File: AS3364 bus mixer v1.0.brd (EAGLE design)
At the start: 44.5 x 30.5 mm, 96 parts, among them IC1 TL072JT, IC2 TL072JT, IC3 TL072JT, IC30 TL072JT, IC4 TL072JT, IC5 79L09F, IC6 78L09F, IC7 CH446Q

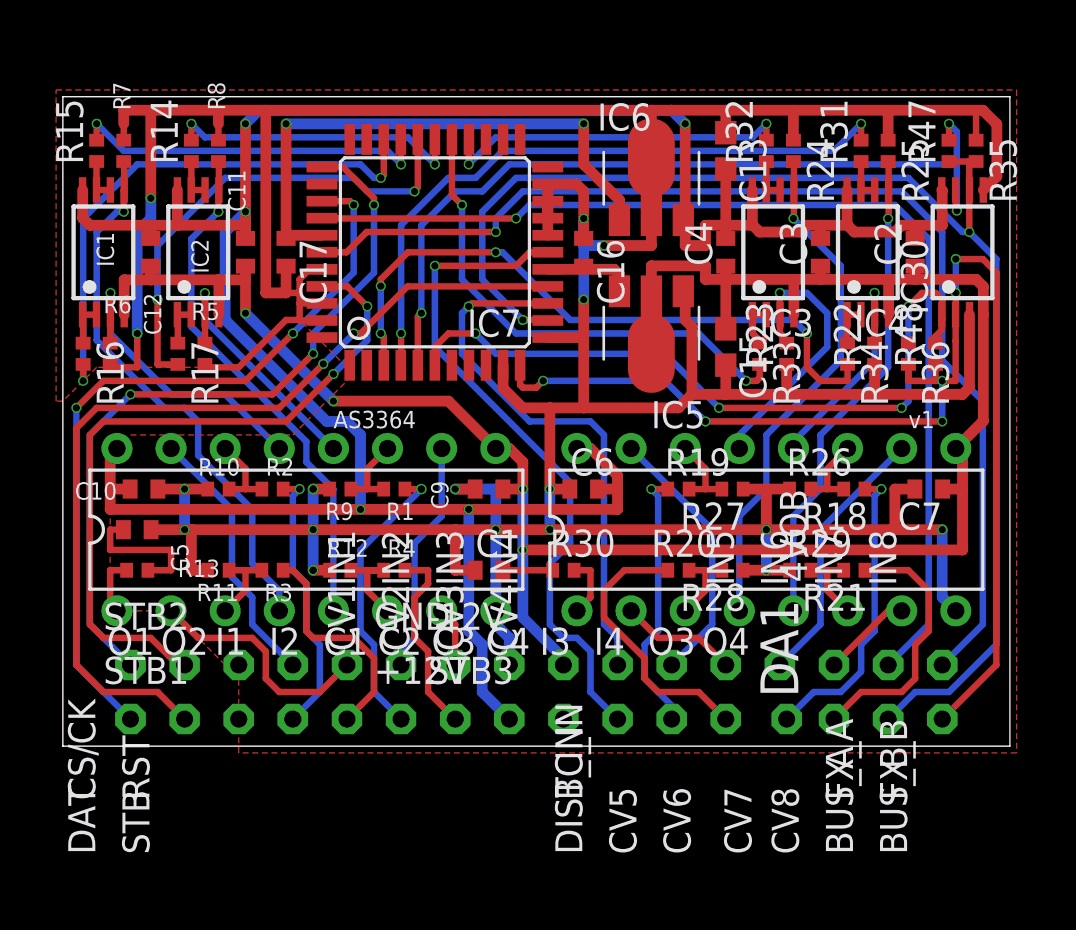
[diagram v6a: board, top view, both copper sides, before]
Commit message: Switched to 16x2 connector
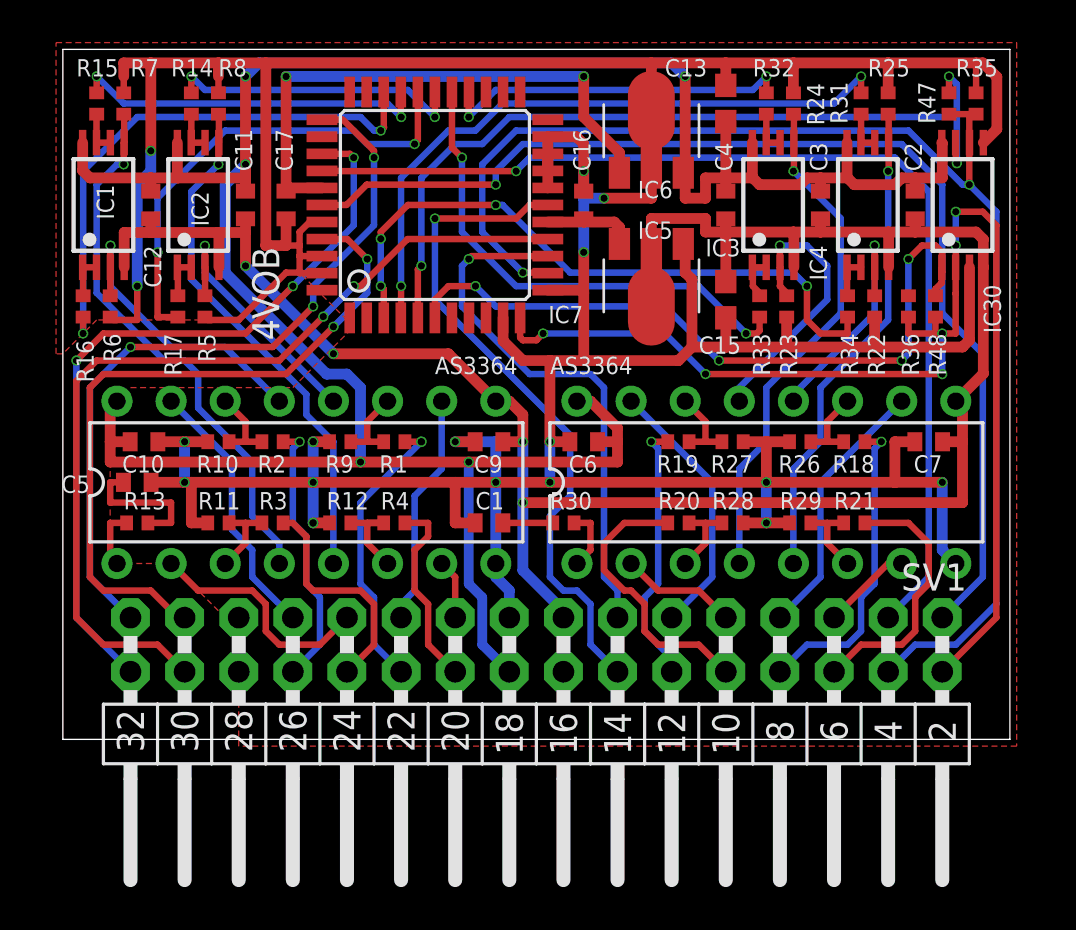
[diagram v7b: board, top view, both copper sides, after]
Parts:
- removed +12V, -12V, BC_IN, BUS_A, BUS_B, CS/CK, CV1, CV2, CV3, CV4, CV5, CV6, CV7, CV8, DAT, DIST_IN, FX_A, FX_B, GND, IN1, IN2, IN3, IN4, IN5, IN6, IN7, IN8, RST, STB, STB1, STB2, STB3: (no value), joakim:MA01NS-1J
- added SV1: (no value), joakim:MA16-2WJ
- U$1: device joakim:XONIK_LOGO_18 -> joakim:XONIK_LOGO_28
- moved U$1 16.3 mm to (36.2, 23.2)
- moved C10 2.22 mm to (3.81, 14.3)
- moved C11 2.22 mm to (8.57, 25.4)
- moved C12 2.22 mm to (4.13, 25.4)
- moved C13 2.22 mm to (31.1, 30.2)
- moved C16 2.22 mm to (24.4, 25.4)
- moved C17 2.22 mm to (10.5, 25.4)
- moved C2 2.22 mm to (40.0, 25.4)
- moved C3 2.22 mm to (35.6, 25.4)
- moved C4 2.22 mm to (31.1, 25.4)
- moved C5 2.22 mm to (3.49, 12.4)
- moved C6 2.22 mm to (24.4, 14.3)
- moved C7 2.22 mm to (40.6, 14.3)
- moved C9 2.22 mm to (20.0, 14.3)
- moved DA1 2.22 mm to (33.0, 12.4)
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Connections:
- net +12V: now also SV1.18; no longer +12V.1
- net -12V: now also IC5.2@1, SV1.15; no longer -12V.1
- net BITCRUSH_IN: now also SV1.13; no longer BC_IN.1
- net BUS_A: now also SV1.4; no longer BUS_A.1
- net BUS_B: now also SV1.2; no longer BUS_B.1
- net CS/CK: now also SV1.31; no longer CS/CK.1
- net CV1: now also SV1.26; no longer CV1.1
- net CV2: now also SV1.24; no longer CV2.1
- net CV3: now also SV1.22; no longer CV3.1
- net CV4: now also SV1.20; no longer CV4.1
- net CV5: now also SV1.12; no longer CV5.1
- net CV6: now also SV1.10; no longer CV6.1
- net CV7: now also SV1.8; no longer CV7.1
- net CV8: now also SV1.6; no longer CV8.1
- net DAT: now also SV1.32; no longer DAT.1
- net DIST_IN: now also SV1.14; no longer DIST_IN.1
- net FX_A: now also SV1.3; no longer FX_A.1
- net FX_B: now also SV1.1; no longer FX_B.1
- net GND: now also SV1.17; no longer GND.1
- net IN1: now also SV1.25; no longer IN1.1
- net IN2: now also SV1.23; no longer IN2.1
- net IN3: now also SV1.21; no longer IN3.1
- net IN4: now also SV1.19; no longer IN4.1
- net IN5: now also SV1.11; no longer IN5.1
- net IN6: now also SV1.9; no longer IN6.1
- net IN7: now also SV1.7; no longer IN7.1
- net IN8: now also SV1.5; no longer IN8.1
- net RST: now also SV1.29; no longer RST.1
- net STB: now also SV1.30; no longer STB.1
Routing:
- net -12V: track 98.9 -> 101.6 mm
- net CV7: track 14.2 -> 14.7 mm
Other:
- board size 44.5 x 30.5 mm -> 44.5 x 32.4 mm
- board text added: "+V"
- board text added: "-V"
- board text added: "BA"
- board text added: "BB"
- board text added: "BC"
- board text added: "C5"
- board text added: "C6"
- board text added: "C7"
- board text added: "C8"
- board text added: "CS"
- board text added: "DS"
- board text added: "DT"
- board text added: "FA"
- board text added: "FB"
- board text added: "G"
- board text added: "I5"
- board text added: "I6"
- board text added: "I7"
- board text added: "I8"
- board text added: "Pre-filter bus mixer v1.0"
- board text added: "RS"
- board text added: "ST"
- board text removed: "+12v"
- board text removed: "-12v"
- board text removed: "AGND"
- board text removed: "NB: Max 26V diff"
- board text removed: "O1"
- board text removed: "O2"
- board text removed: "O3"
- board text removed: "O4"
- board text removed: "Quad linear VCA"
- board text removed: "v1"
